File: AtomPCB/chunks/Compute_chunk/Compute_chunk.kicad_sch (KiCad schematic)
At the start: 33 parts, among them J1 DF40C-40DP-0.4V_51_, U1 USBLC6-2SC6, U2 ESP32-S3-WROOM-1U-N8R8, U3 MPM3610AGQV-P, U4 SN74HCT125DR, U6 MPM3610AGQV-P

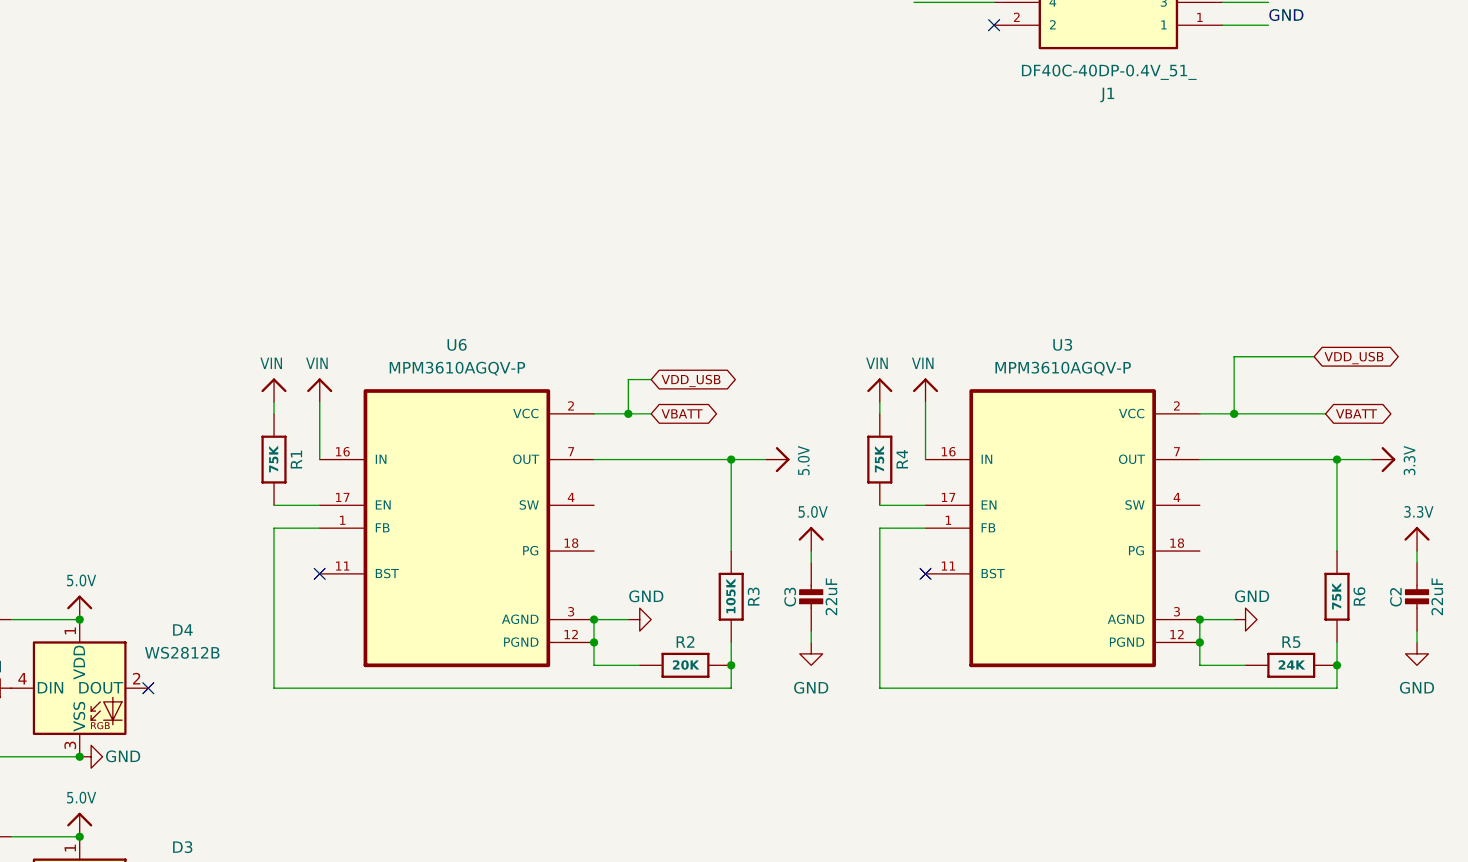
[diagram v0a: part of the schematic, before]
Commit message: updated compute chunk schematic to introduce missing resistor and capacitor. Changed diff resistor values on 3v3 buck
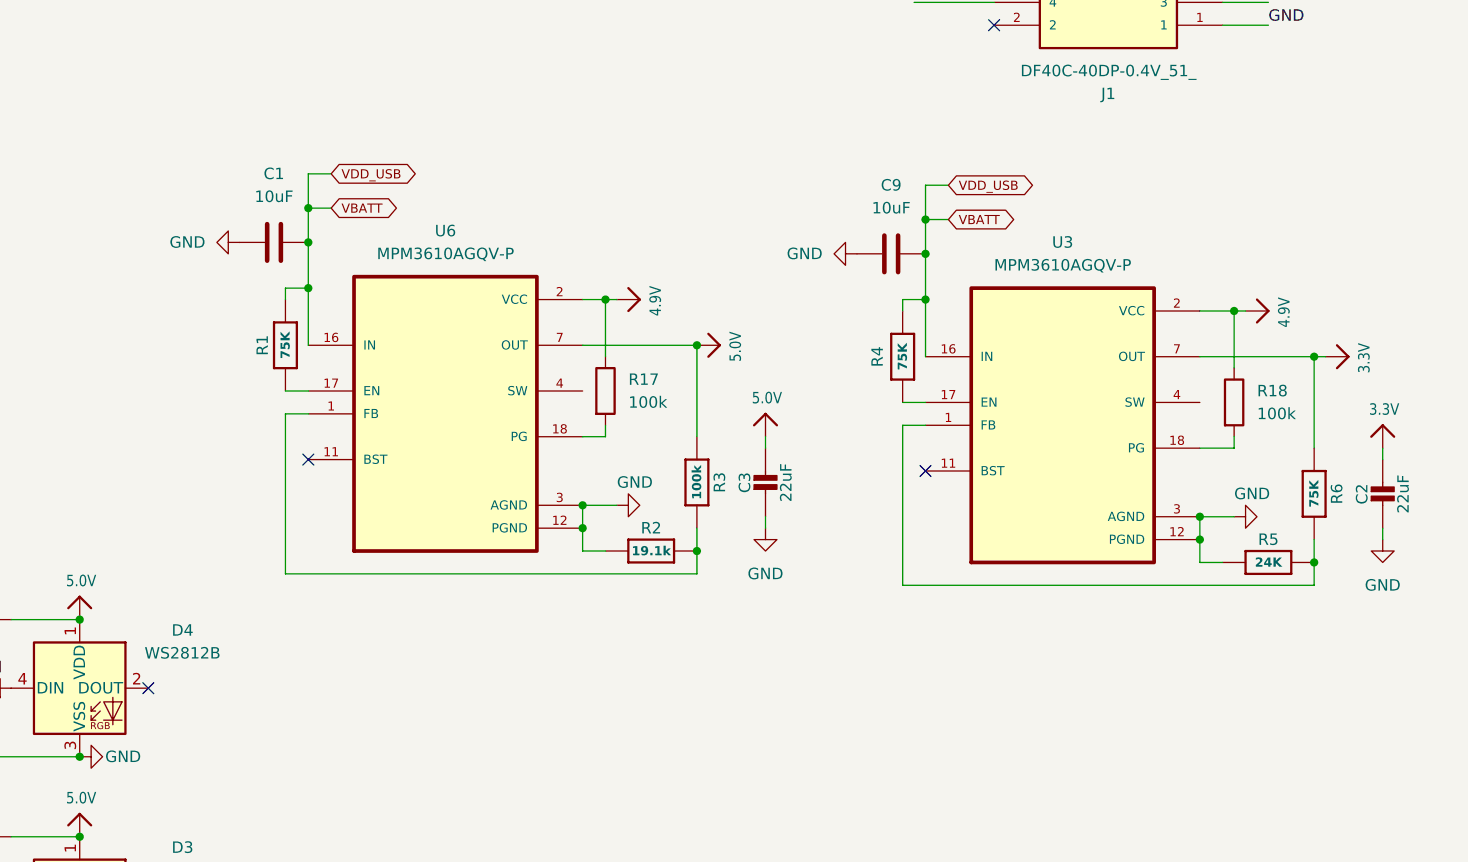
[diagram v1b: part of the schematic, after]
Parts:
- added C1, C9: 10uF, Capacitor_SMD:C_0805_2012Metric, symbol Device:C
- added R17, R18: 100k, Resistor_SMD:R_0805_2012Metric, symbol Device:R
- R2: value 20K -> 19.1k
- R3: value 105K -> 100k
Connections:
- net VIN is gone; now on net VBATT: R1.1, R4.1, U3.16 (IN), U6.16 (IN)
- net GND: now also C1.1, C9.1
- net VBATT: now also C1.2, C9.2; no longer U3.2 (VCC), U6.2 (VCC)
- net at U6.18 (PG): now also R17.2
- net at U3.18 (PG): now also R18.2
- new net 4.9V: R17.1, R18.1, U3.2 (VCC), U6.2 (VCC)
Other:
- moved on the sheet: C2, C3, R1, R2, R3, R4, R5, R6, U3, U6
